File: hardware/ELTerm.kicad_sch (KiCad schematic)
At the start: 31 parts, among them J1 Barrel_Jack_Switch, J2 Conn_02x10_Odd_Even, J3 Conn_01x02, J4 Mini-DIN-6, J5 Conn_02x03_Odd_Even, J6 Conn_01x02, J7 DB9_Male_MountingHoles, SW1 SW_Push, U1 SY8120, U2 Pico, U3 MAX3232, U4 NC7WZ16P6X

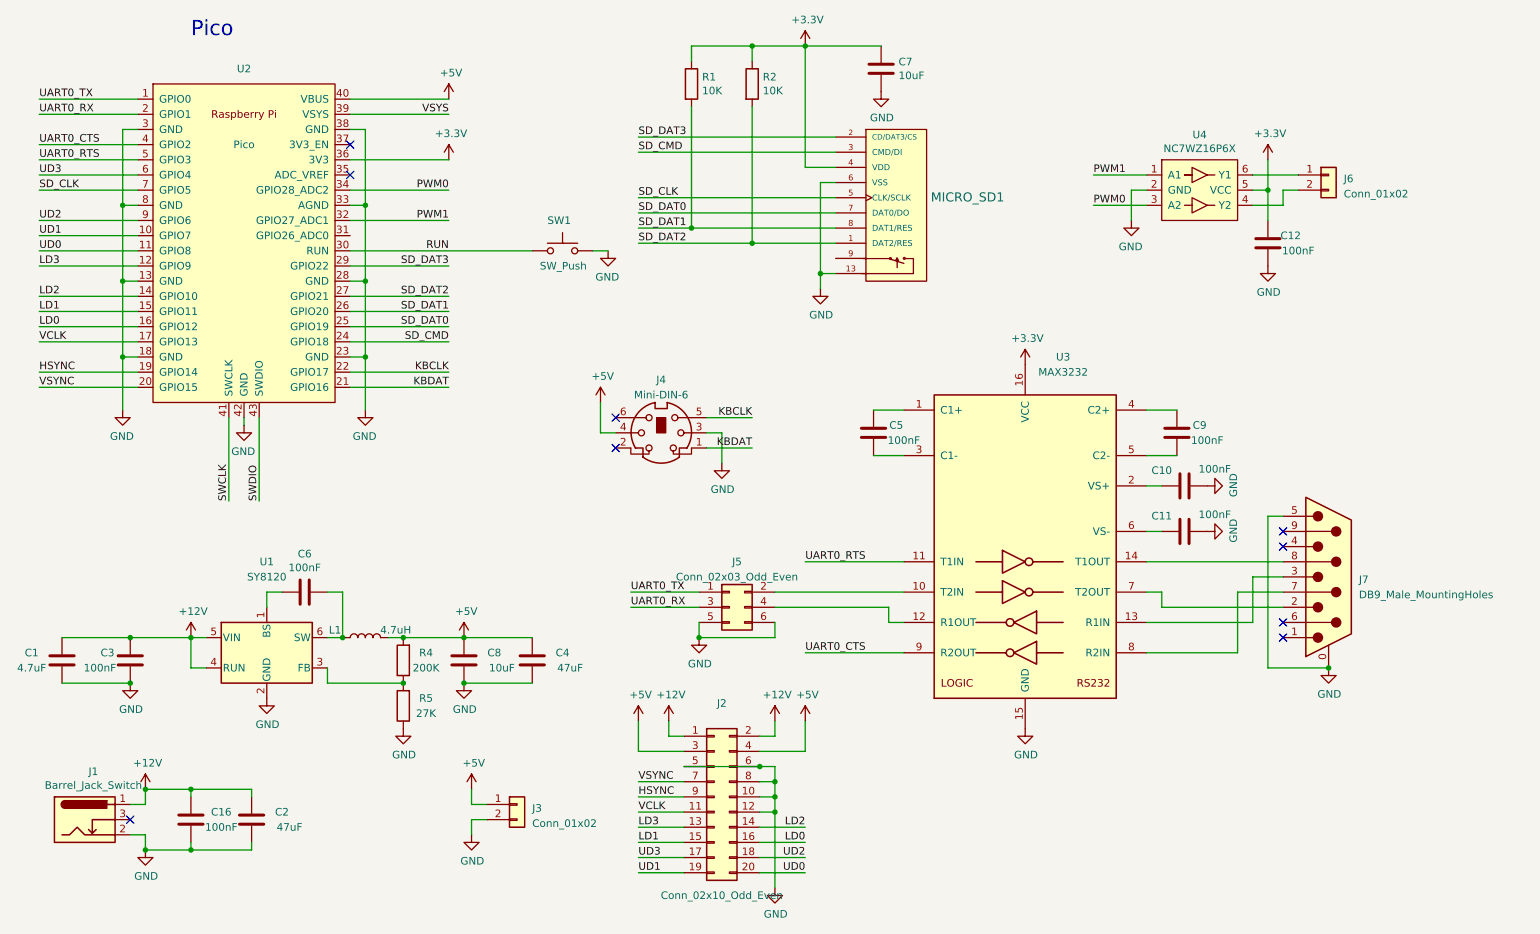
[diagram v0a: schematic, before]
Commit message: - Fix PCB EL pin assignment
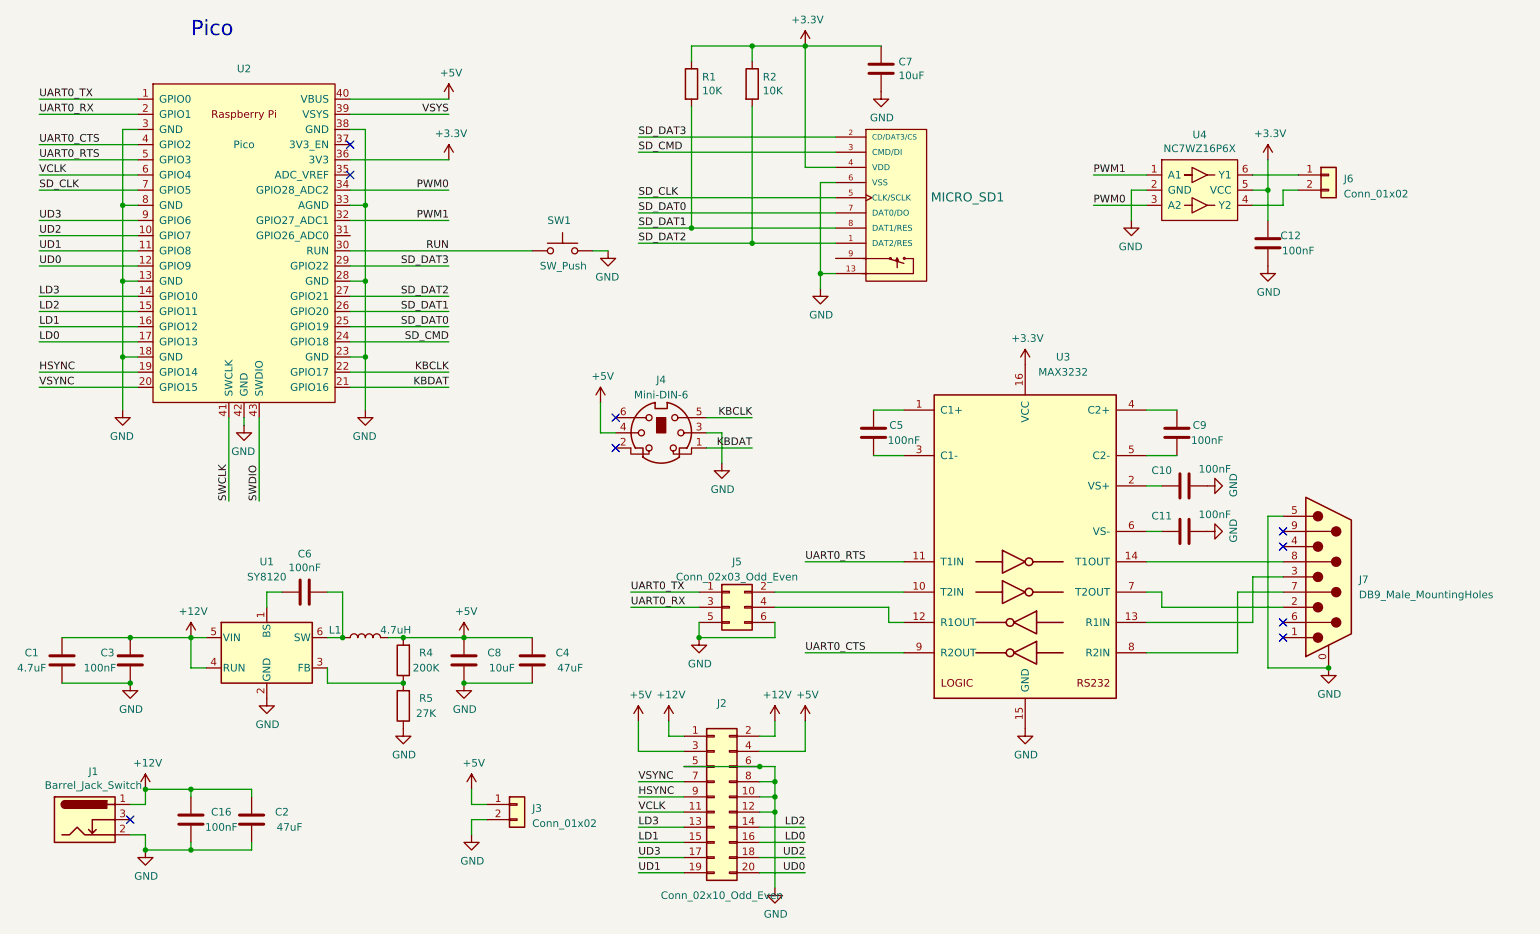
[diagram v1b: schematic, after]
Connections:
- net LD0: now also U2.17 (GPIO13); no longer U2.16 (GPIO12)
- net LD1: now also U2.16 (GPIO12); no longer U2.15 (GPIO11)
- net LD2: now also U2.15 (GPIO11); no longer U2.14 (GPIO10)
- net LD3: now also U2.14 (GPIO10); no longer U2.12 (GPIO9)
- net UD0: now also U2.12 (GPIO9); no longer U2.11 (GPIO8)
- net UD1: now also U2.11 (GPIO8); no longer U2.10 (GPIO7)
- net UD2: now also U2.10 (GPIO7); no longer U2.9 (GPIO6)
- net UD3: now also U2.9 (GPIO6); no longer U2.6 (GPIO4)
- net VCLK: now also U2.6 (GPIO4); no longer U2.17 (GPIO13)
